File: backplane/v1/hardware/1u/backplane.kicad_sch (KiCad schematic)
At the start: 1 part, among them J1 Conn_02x20_Odd_Even

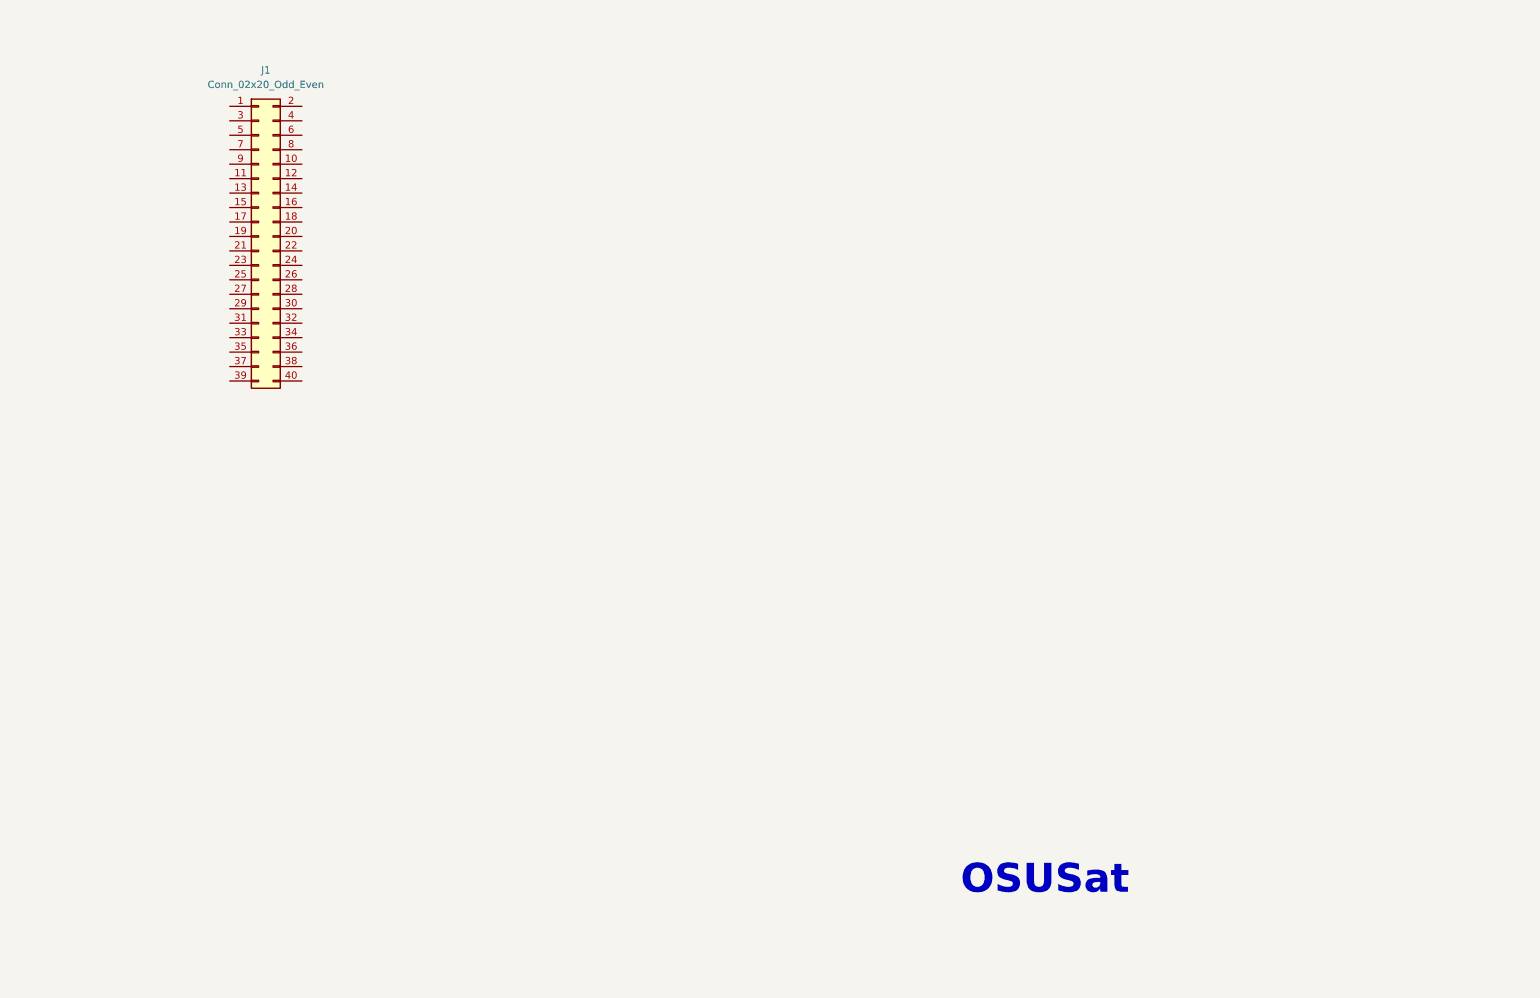
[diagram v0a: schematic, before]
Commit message: add pinout documentation
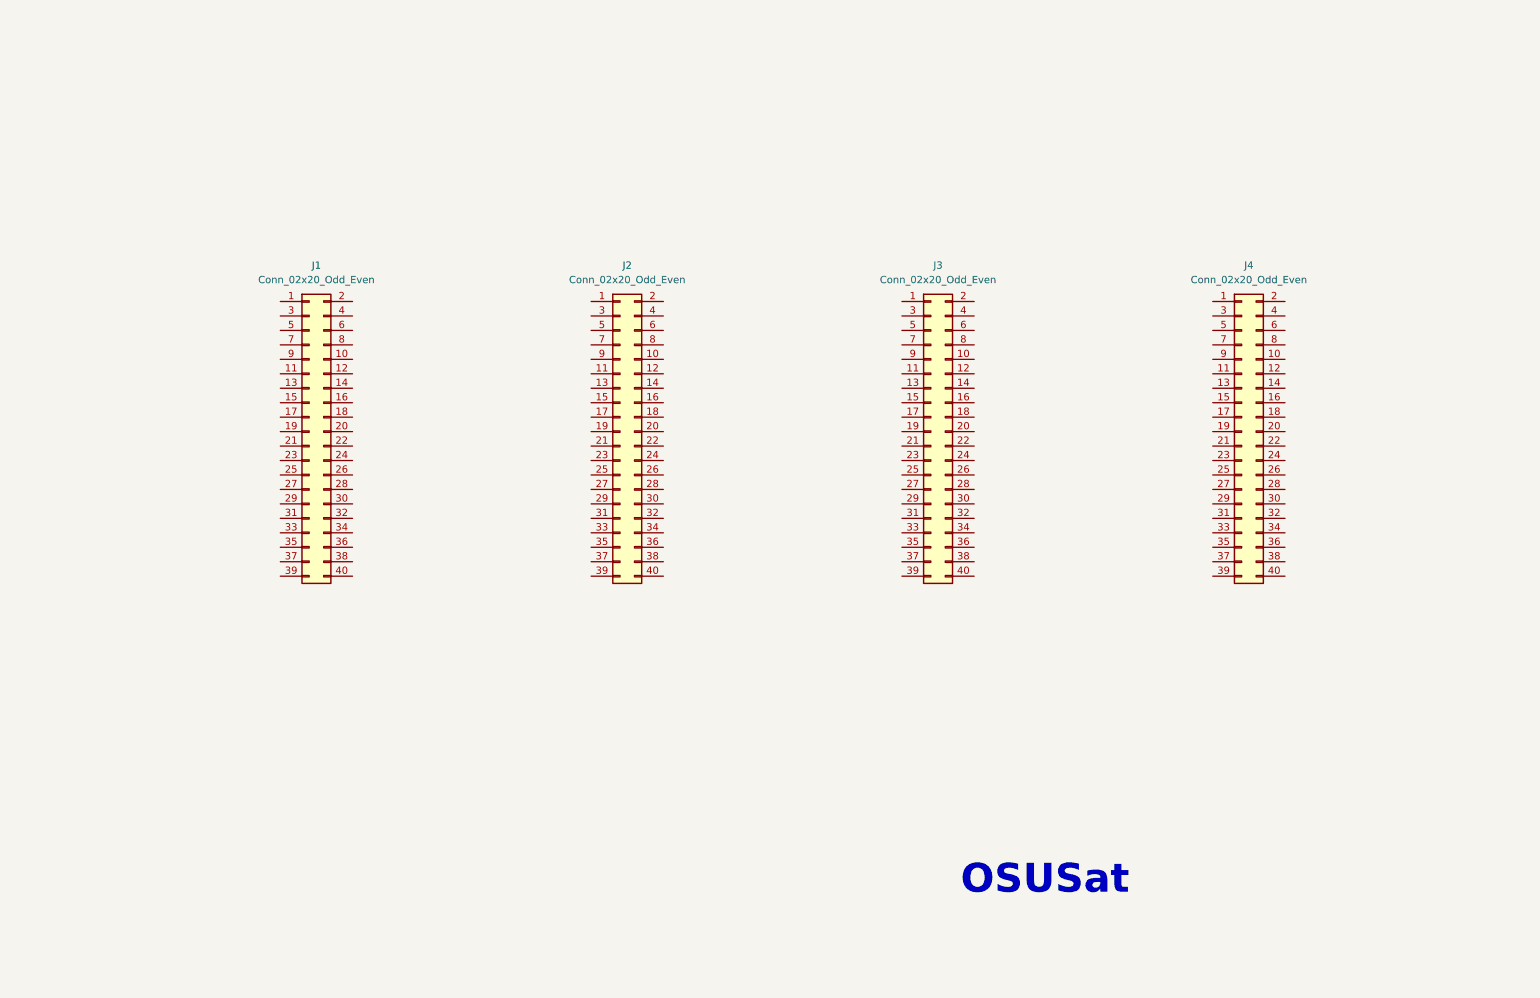
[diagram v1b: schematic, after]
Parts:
- added J2, J3, J4: Conn_02x20_Odd_Even, symbol Connector_Generic:Conn_02x20_Odd_Even
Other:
- moved on the sheet: J1

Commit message: add mechanical constraints
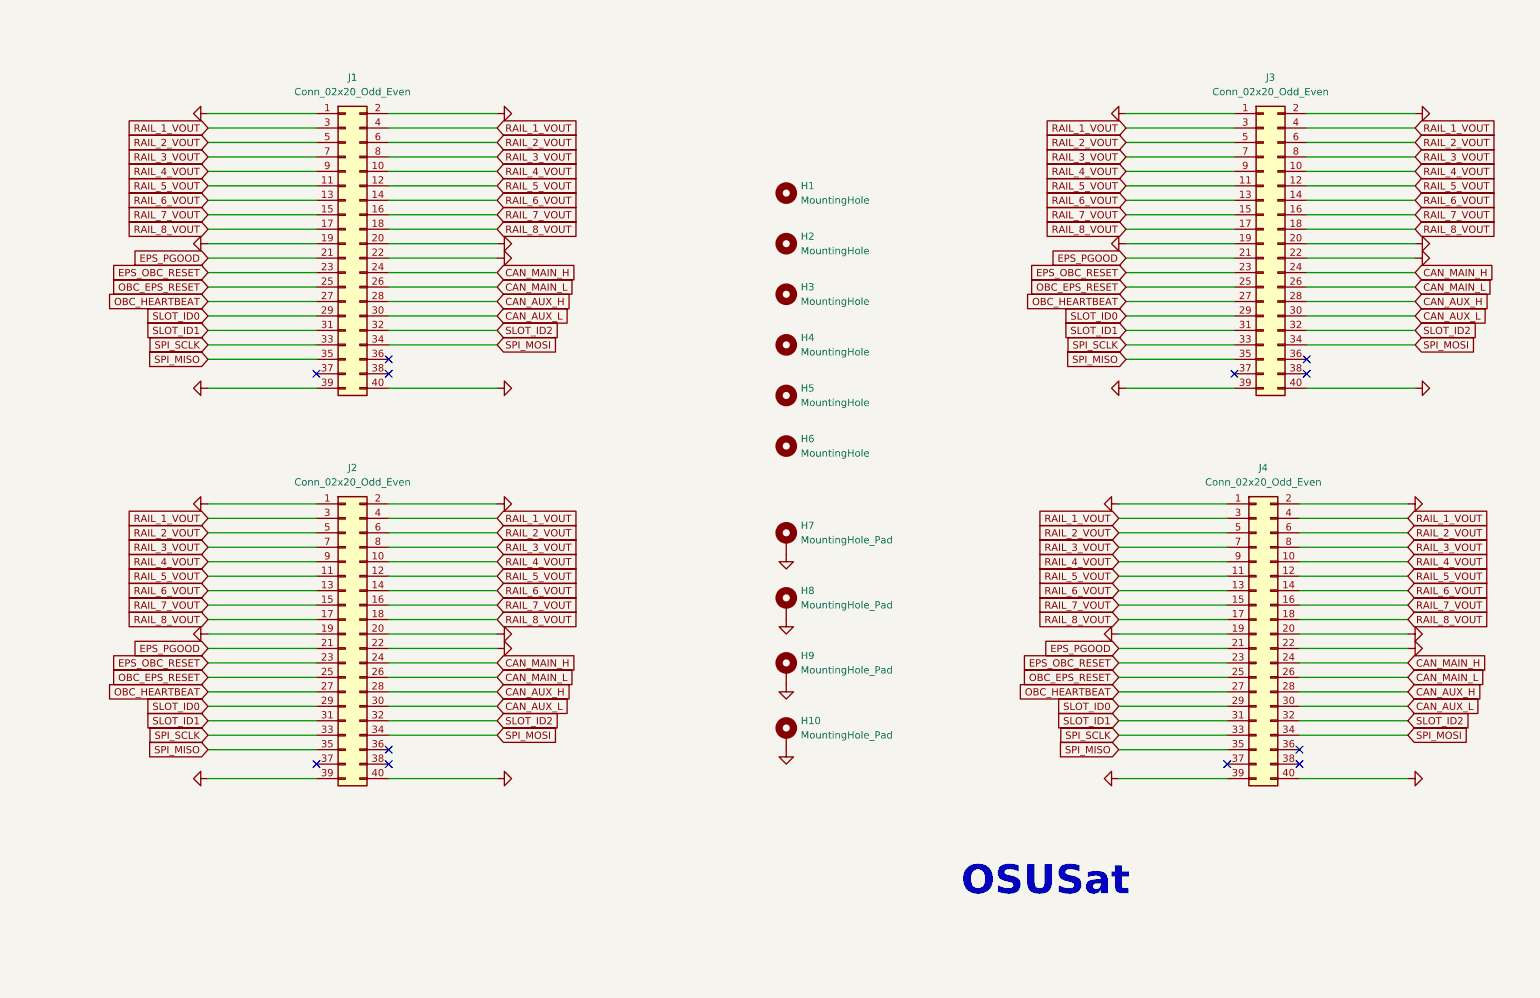
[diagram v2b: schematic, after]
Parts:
- added H1, H2, H3, H4, H5, H6: MountingHole, MountingHole:MountingHole_4.3mm_M4, symbol Mechanical:MountingHole
- added H10, H7, H8, H9: MountingHole_Pad, MountingHole:MountingHole_3.2mm_M3_Pad, symbol Mechanical:MountingHole_Pad
- J1, J2, J3, J4: footprint (none) -> footprints:SAMTEC_SFM-120-01-L-D-A-TR
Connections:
- net GND: now reaches J4.1 (Pin_1)
- net GND: now also J1.1 (Pin_1), J1.19 (Pin_19), J1.2 (Pin_2), J1.20 (Pin_20), J1.22 (Pin_22), J1.39 (Pin_39), J1.40 (Pin_40), J2.1 (Pin_1), J2.19 (Pin_19), J2.2 (Pin_2), J2.20 (Pin_20), J2.22 (Pin_22), J2.39 (Pin_39), J2.40 (Pin_40), J3.1 (Pin_1), J3.19 (Pin_19), J3.2 (Pin_2), J3.20 (Pin_20), J3.22 (Pin_22), J3.39 (Pin_39), J3.40 (Pin_40), J4.19 (Pin_19), J4.2 (Pin_2), J4.20 (Pin_20), J4.22 (Pin_22), J4.39 (Pin_39), J4.40 (Pin_40), H10.1, H7.1, H8.1, H9.1
- net RAIL_4_VOUT: now reaches J4.10 (Pin_10)
- net RAIL_4_VOUT: now also J1.10 (Pin_10), J1.9 (Pin_9), J2.10 (Pin_10), J2.9 (Pin_9), J3.10 (Pin_10), J3.9 (Pin_9), J4.9 (Pin_9)
- net RAIL_5_VOUT: now reaches J4.11 (Pin_11)
- net RAIL_5_VOUT: now also J1.11 (Pin_11), J1.12 (Pin_12), J2.11 (Pin_11), J2.12 (Pin_12), J3.11 (Pin_11), J3.12 (Pin_12), J4.12 (Pin_12)
- net RAIL_6_VOUT: now reaches J4.13 (Pin_13)
- net RAIL_6_VOUT: now also J1.13 (Pin_13), J1.14 (Pin_14), J2.13 (Pin_13), J2.14 (Pin_14), J3.13 (Pin_13), J3.14 (Pin_14), J4.14 (Pin_14)
- net RAIL_7_VOUT: now reaches J4.15 (Pin_15)
- net RAIL_7_VOUT: now also J1.15 (Pin_15), J1.16 (Pin_16), J2.15 (Pin_15), J2.16 (Pin_16), J3.15 (Pin_15), J3.16 (Pin_16), J4.16 (Pin_16)
- net RAIL_8_VOUT: now reaches J4.17 (Pin_17)
- net RAIL_8_VOUT: now also J1.17 (Pin_17), J1.18 (Pin_18), J2.17 (Pin_17), J2.18 (Pin_18), J3.17 (Pin_17), J3.18 (Pin_18), J4.18 (Pin_18)
- net EPS_PGOOD: now reaches J4.21 (Pin_21)
- net EPS_PGOOD: now also J1.21 (Pin_21), J2.21 (Pin_21), J3.21 (Pin_21)
- net EPS_OBC_RESET: now reaches J4.23 (Pin_23)
- net EPS_OBC_RESET: now also J1.23 (Pin_23), J2.23 (Pin_23), J3.23 (Pin_23)
- net CAN_MAIN_H: now reaches J4.24 (Pin_24)
- net CAN_MAIN_H: now also J1.24 (Pin_24), J2.24 (Pin_24), J3.24 (Pin_24)
- net OBC_EPS_RESET: now reaches J4.25 (Pin_25)
- net OBC_EPS_RESET: now also J1.25 (Pin_25), J2.25 (Pin_25), J3.25 (Pin_25)
- net CAN_MAIN_L: now reaches J4.26 (Pin_26)
- net CAN_MAIN_L: now also J1.26 (Pin_26), J2.26 (Pin_26), J3.26 (Pin_26)
- net OBC_HEARTBEAT: now reaches J4.27 (Pin_27)
- net OBC_HEARTBEAT: now also J1.27 (Pin_27), J2.27 (Pin_27), J3.27 (Pin_27)
- net CAN_AUX_H: now reaches J4.28 (Pin_28)
- net CAN_AUX_H: now also J1.28 (Pin_28), J2.28 (Pin_28), J3.28 (Pin_28)
- net SLOT_ID0: now reaches J4.29 (Pin_29)
- net SLOT_ID0: now also J1.29 (Pin_29), J2.29 (Pin_29), J3.29 (Pin_29)
- net RAIL_1_VOUT: now reaches J4.3 (Pin_3)
- net RAIL_1_VOUT: now also J1.3 (Pin_3), J1.4 (Pin_4), J2.3 (Pin_3), J2.4 (Pin_4), J3.3 (Pin_3), J3.4 (Pin_4), J4.4 (Pin_4)
- net CAN_AUX_L: now reaches J4.30 (Pin_30)
- net CAN_AUX_L: now also J1.30 (Pin_30), J2.30 (Pin_30), J3.30 (Pin_30)
- net SLOT_ID1: now reaches J4.31 (Pin_31)
- net SLOT_ID1: now also J1.31 (Pin_31), J2.31 (Pin_31), J3.31 (Pin_31)
- net SLOT_ID2: now reaches J4.32 (Pin_32)
- net SLOT_ID2: now also J1.32 (Pin_32), J2.32 (Pin_32), J3.32 (Pin_32)
- net SPI_SCLK: now reaches J4.33 (Pin_33)
- net SPI_SCLK: now also J1.33 (Pin_33), J2.33 (Pin_33), J3.33 (Pin_33)
- net SPI_MOSI: now reaches J4.34 (Pin_34)
- net SPI_MOSI: now also J1.34 (Pin_34), J2.34 (Pin_34), J3.34 (Pin_34)
- net SPI_MISO: now reaches J4.35 (Pin_35)
- net SPI_MISO: now also J1.35 (Pin_35), J2.35 (Pin_35), J3.35 (Pin_35)
- net RAIL_2_VOUT: now reaches J4.5 (Pin_5)
- net RAIL_2_VOUT: now also J1.5 (Pin_5), J1.6 (Pin_6), J2.5 (Pin_5), J2.6 (Pin_6), J3.5 (Pin_5), J3.6 (Pin_6), J4.6 (Pin_6)
- net RAIL_3_VOUT: now reaches J4.7 (Pin_7)
- net RAIL_3_VOUT: now also J1.7 (Pin_7), J1.8 (Pin_8), J2.7 (Pin_7), J2.8 (Pin_8), J3.7 (Pin_7), J3.8 (Pin_8), J4.8 (Pin_8)
- no-connect marks 0 -> 12
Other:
- moved on the sheet: J1, J2, J3, J4

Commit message: finish preliminary 1U design
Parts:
- J1, J2, J3, J4: footprint footprints:SAMTEC_SFM-120-01-L-D-A-TR -> footprints:SFM-120-X1-XXX-D
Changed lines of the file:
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@@
 			)
 		)
-		(property "Footprint" "footprints:SAMTEC_SFM-120-01-L-D-A-TR"
+		(property "Footprint" "footprints:SFM-120-X1-XXX-D"
 			(at 228.6 134.62 0)
 			(hide yes)
@@
 			)
 		)
-		(property "Footprint" "footprints:SAMTEC_SFM-120-01-L-D-A-TR"
+		(property "Footprint" "footprints:SFM-120-X1-XXX-D"
 			(at 68.58 66.04 0)
 			(hide yes)
@@
 			)
 		)
-		(property "Footprint" "footprints:SAMTEC_SFM-120-01-L-D-A-TR"
+		(property "Footprint" "footprints:SFM-120-X1-XXX-D"
 			(at 68.58 134.62 0)
 			(hide yes)
@@
 			)
 		)
-		(property "Footprint" "footprints:SAMTEC_SFM-120-01-L-D-A-TR"
+		(property "Footprint" "footprints:SFM-120-X1-XXX-D"
 			(at 229.87 66.04 0)
 			(hide yes)

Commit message: revisions from design review
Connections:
- net GND: now also J1.LC1, J1.LC2, J2.LC1, J2.LC2, J3.LC1, J3.LC2, J4.LC1, J4.LC2
- net SPARE1: now reaches J4.36 (Pin_36)
- net SPARE1: now also J1.36 (Pin_36), J2.36 (Pin_36), J3.36 (Pin_36)
- net SPARE2: now reaches J4.37 (Pin_37)
- net SPARE2: now also J1.37 (Pin_37), J2.37 (Pin_37), J3.37 (Pin_37)
- net SPARE3: now reaches J4.38 (Pin_38)
- net SPARE3: now also J1.38 (Pin_38), J2.38 (Pin_38), J3.38 (Pin_38)
- no-connect marks 12 -> 0
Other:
- note added: "BAT"
- note added: "COMM"
- note added: "EPS"
- note added: "OBC"
- moved on the sheet: H10, H7, H8, H9

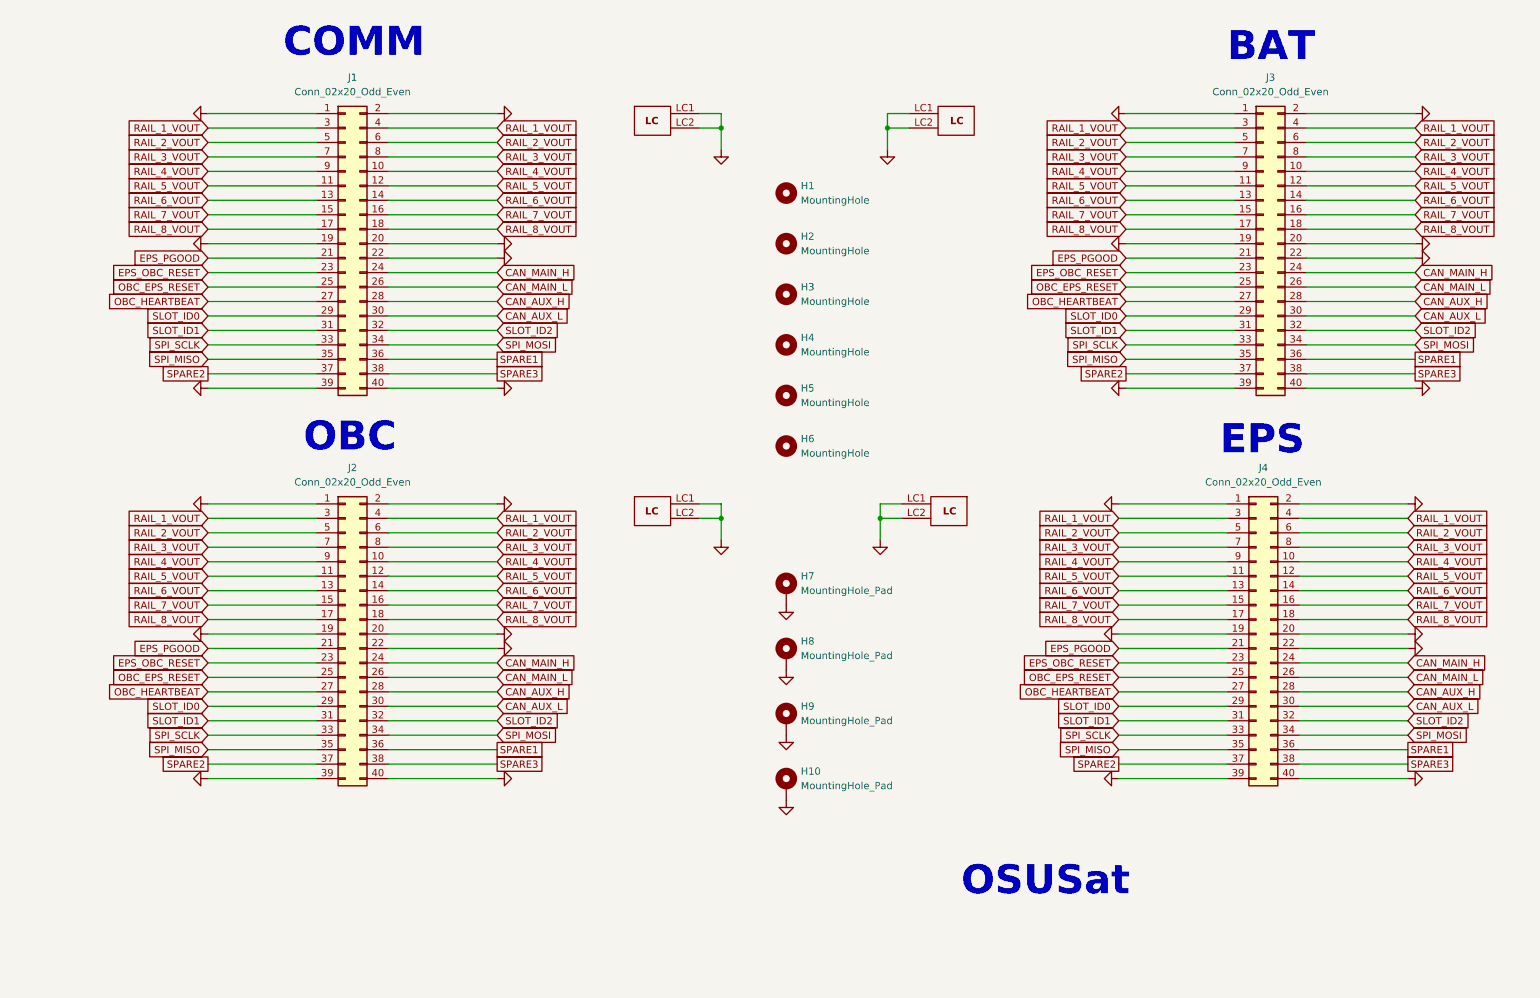
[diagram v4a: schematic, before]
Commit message: route main CANBus line as differential pair
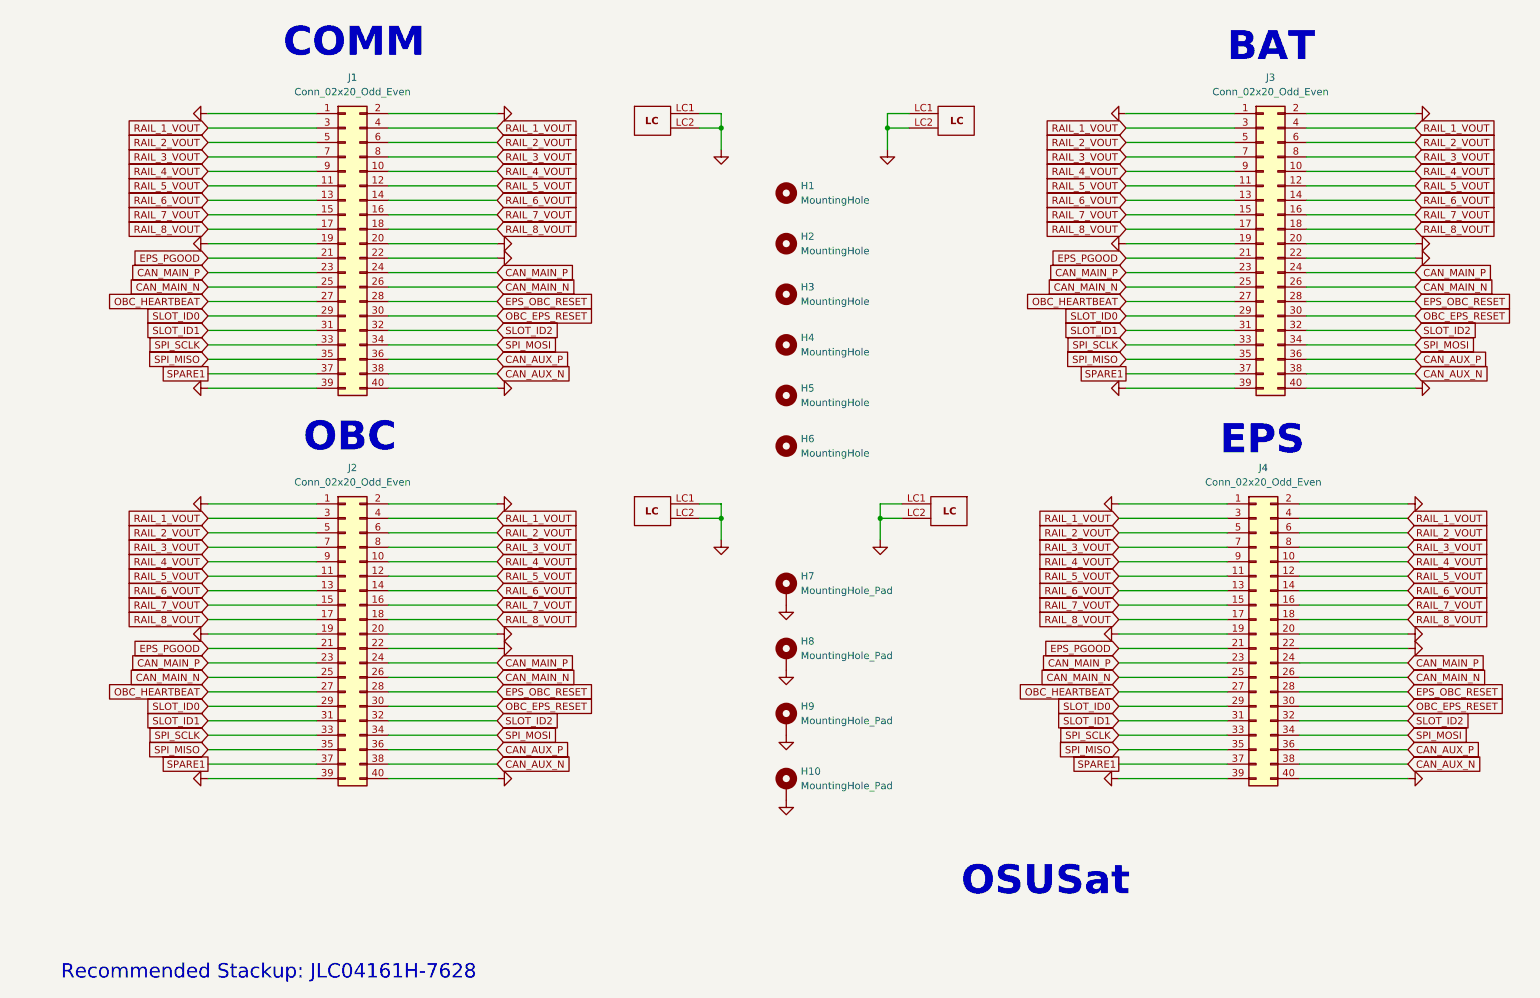
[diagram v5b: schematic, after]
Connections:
- net CAN_AUX_H is gone; now on net EPS_OBC_RESET: J1.28 (Pin_28), J2.28 (Pin_28), J3.28 (Pin_28), J4.28 (Pin_28)
- net CAN_AUX_L is gone; now on net OBC_EPS_RESET: J1.30 (Pin_30), J2.30 (Pin_30), J3.30 (Pin_30), J4.30 (Pin_30)
- net SPARE2 is gone; now on net SPARE1: J1.37 (Pin_37), J2.37 (Pin_37), J3.37 (Pin_37), J4.37 (Pin_37)
- net EPS_OBC_RESET: no longer J1.23 (Pin_23), J2.23 (Pin_23), J3.23 (Pin_23), J4.23 (Pin_23)
- net OBC_EPS_RESET: no longer J1.25 (Pin_25), J2.25 (Pin_25), J3.25 (Pin_25), J4.25 (Pin_25)
- net SPARE1: no longer J1.36 (Pin_36), J2.36 (Pin_36), J3.36 (Pin_36), J4.36 (Pin_36)
- net CAN_MAIN_H renamed CAN_MAIN_P
- net CAN_MAIN_P: now also J1.23 (Pin_23), J2.23 (Pin_23), J3.23 (Pin_23), J4.23 (Pin_23)
- net CAN_MAIN_L renamed CAN_MAIN_N
- net CAN_MAIN_N: now also J1.25 (Pin_25), J2.25 (Pin_25), J3.25 (Pin_25), J4.25 (Pin_25)
- net SPARE3 renamed CAN_AUX_N
- new net CAN_AUX_P: J1.36 (Pin_36), J2.36 (Pin_36), J3.36 (Pin_36), J4.36 (Pin_36)
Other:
- note added: "Recommended Stackup: JLC04161H-7628"
